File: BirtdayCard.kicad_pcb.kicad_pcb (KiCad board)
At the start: 2 copper layers, 26 parts, among them U2 0.763V~7V 4.2V~18V 3A, U3 ESP32-WROOM-32D-N4

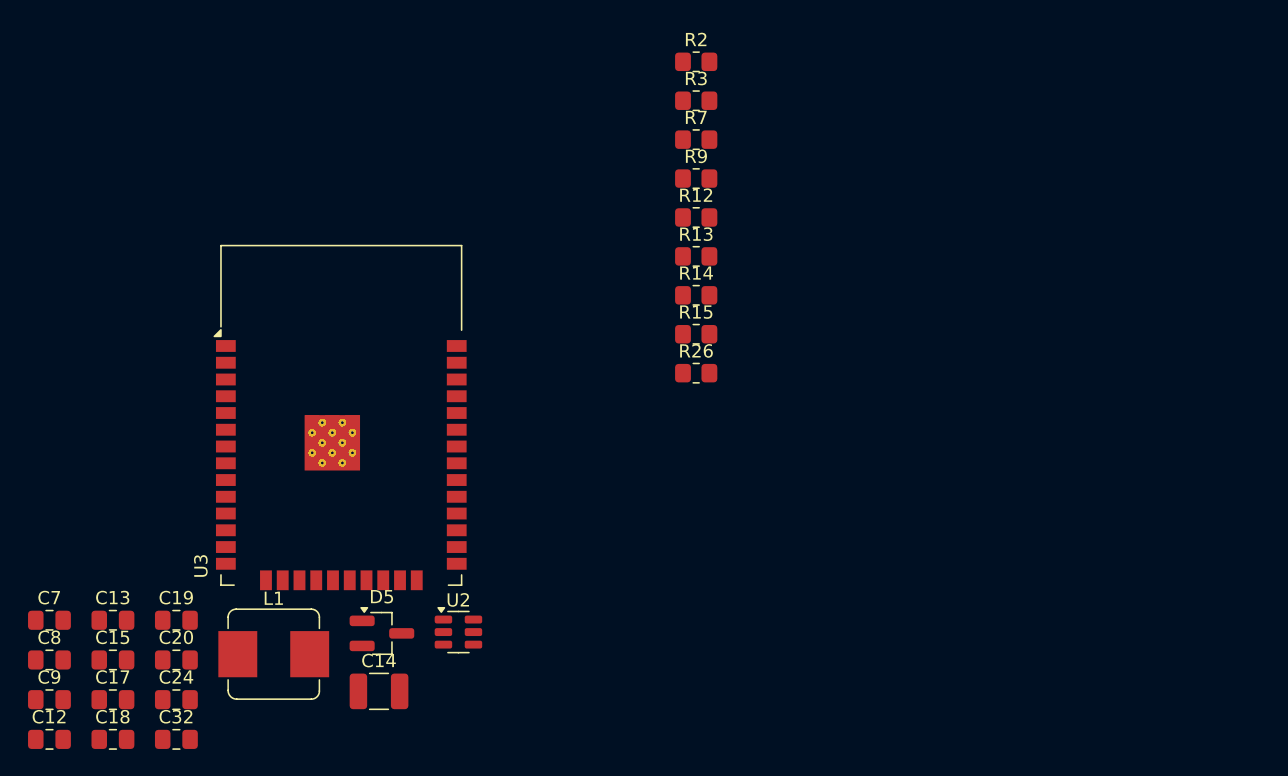
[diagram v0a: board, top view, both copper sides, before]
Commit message: adding components and consolidating with current parts
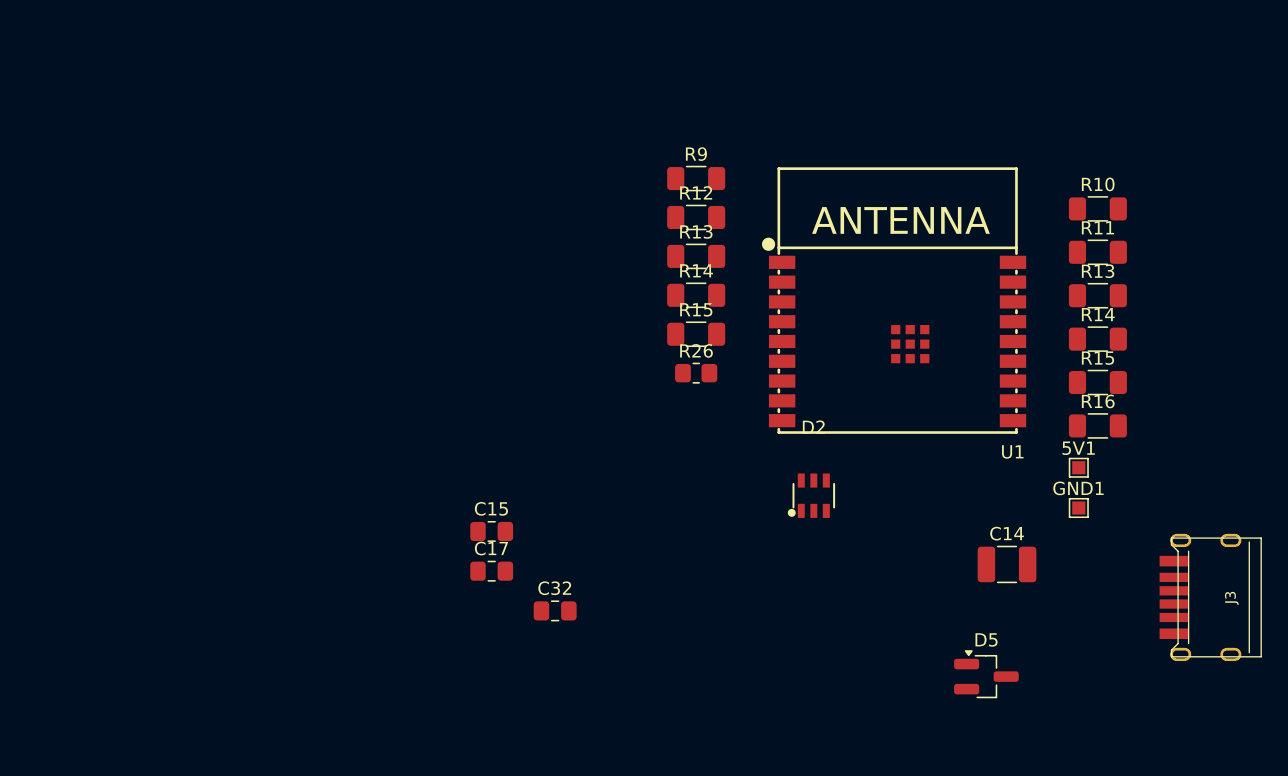
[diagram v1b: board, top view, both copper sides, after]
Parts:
- removed C12, C18, C19, C20, C7, C8: 10uF 25V, Capacitor_SMD:C_0805_2012Metric_Pad1.18x1.45mm_HandSolder
- removed C13: 470nF 50V, Capacitor_SMD:C_0805_2012Metric_Pad1.18x1.45mm_HandSolder
- removed C24, C9: 100nF 50V, Capacitor_SMD:C_0805_2012Metric_Pad1.18x1.45mm_HandSolder
- removed L1: 3.3uH 6A, Inductor_SMD:L_Bourns_SRP7028A_7.3x6.6mm
- removed R2: 33.2k, Resistor_SMD:R_0805_2012Metric_Pad1.20x1.40mm_HandSolder
- removed R3, R7: 10k, Resistor_SMD:R_0805_2012Metric_Pad1.20x1.40mm_HandSolder
- removed U2: 0.763V~7V 4.2V~18V 3A, Package_TO_SOT_SMD:TSOT-23-6
- removed U3: ESP32-WROOM-32D-N4, RF_Module:ESP32-WROOM-32
- added 5V1: 5V, TestPoint:TestPoint_Pad_1.0x1.0mm, F.Cu at (139.0, 79.7)
- added D2: USBLC6-2SC6, easyeda2kicad:SOT-23-6_L2.9-W1.6-P0.95-LS2.8-BL, F.Cu at (118.9, 81.8)
- added GND1: GND, TestPoint:TestPoint_Pad_1.0x1.0mm, F.Cu at (139.0, 82.7)
- added J3: USB_C_Receptacle_USB2.0, USB-C-Power-tester:TYPE-C-31-M-17_handsolder, F.Cu at (150.5, 89.5)
- added R10: 10k, Resistor_SMD:R_1206_3216Metric_Pad1.30x1.75mm_HandSolder, F.Cu at (140.4, 60.0)
- added R11: 10k, Resistor_SMD:R_1206_3216Metric_Pad1.30x1.75mm_HandSolder, F.Cu at (140.4, 63.3)
- added R13: 5k1, Resistor_SMD:R_1206_3216Metric_Pad1.30x1.75mm_HandSolder, F.Cu at (140.4, 66.6)
- added R14: 10k, Resistor_SMD:R_1206_3216Metric_Pad1.30x1.75mm_HandSolder, F.Cu at (140.4, 69.9)
- added R15: 10k, Resistor_SMD:R_1206_3216Metric_Pad1.30x1.75mm_HandSolder, F.Cu at (140.4, 73.2)
- added R16: 5k1, Resistor_SMD:R_1206_3216Metric_Pad1.30x1.75mm_HandSolder, F.Cu at (140.4, 76.5)
- added U1: ESP32-C3-WROOM-02-N4(4MB), easyeda2kicad:BULETM-SMD_ESPRESSIF_ESP32-C3-WROOM-02-N4-4MB, F.Cu at (125.3, 70.1)
- R12, R9: footprint Resistor_SMD:R_0805_2012Metric_Pad1.20x1.40mm_HandSolder -> Resistor_SMD:R_1206_3216Metric_Pad1.30x1.75mm_HandSolder
- R13: value 10k -> 5k1; footprint Resistor_SMD:R_0805_2012Metric_Pad1.20x1.40mm_HandSolder -> Resistor_SMD:R_1206_3216Metric_Pad1.30x1.75mm_HandSolder
- R14, R15: value 4.7k -> 10k; footprint Resistor_SMD:R_0805_2012Metric_Pad1.20x1.40mm_HandSolder -> Resistor_SMD:R_1206_3216Metric_Pad1.30x1.75mm_HandSolder
- moved C14 48.6 mm to (133.6, 87.0)
- moved D5 45.9 mm to (132.0, 95.5)
- moved C32 30.3 mm to (99.3, 90.5)
- moved C15 30.3 mm to (94.5, 84.5)
- moved C17 30.3 mm to (94.5, 87.5)
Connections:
- D5 pad 1: GPIO22 -> GPIO7
- D5 pad 2: GPIO21 -> GPIO6
- R12 pad 2: GPIO13 -> GPIO3
- R13 pad 1: GPIO0 -> GND
- R13 pad 2: +3V3 -> Net-(J3-CC1)
- R14 pad 1: GPIO22 -> +3V3
- R14 pad 2: +3V3 -> GPIO8
- R15 pad 1: GPIO21 -> +3V3
- R15 pad 2: +3V3 -> ESP_EN

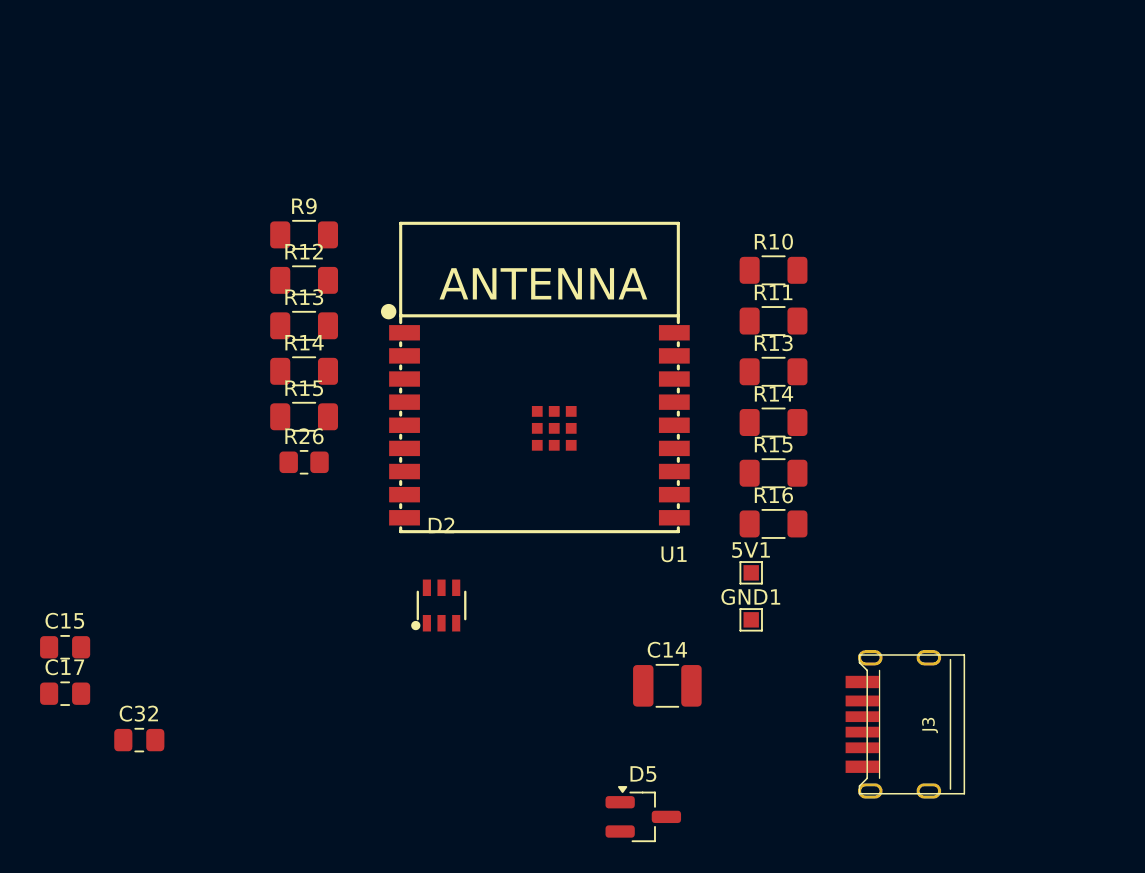
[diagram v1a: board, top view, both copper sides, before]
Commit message: USB configured and added LDO
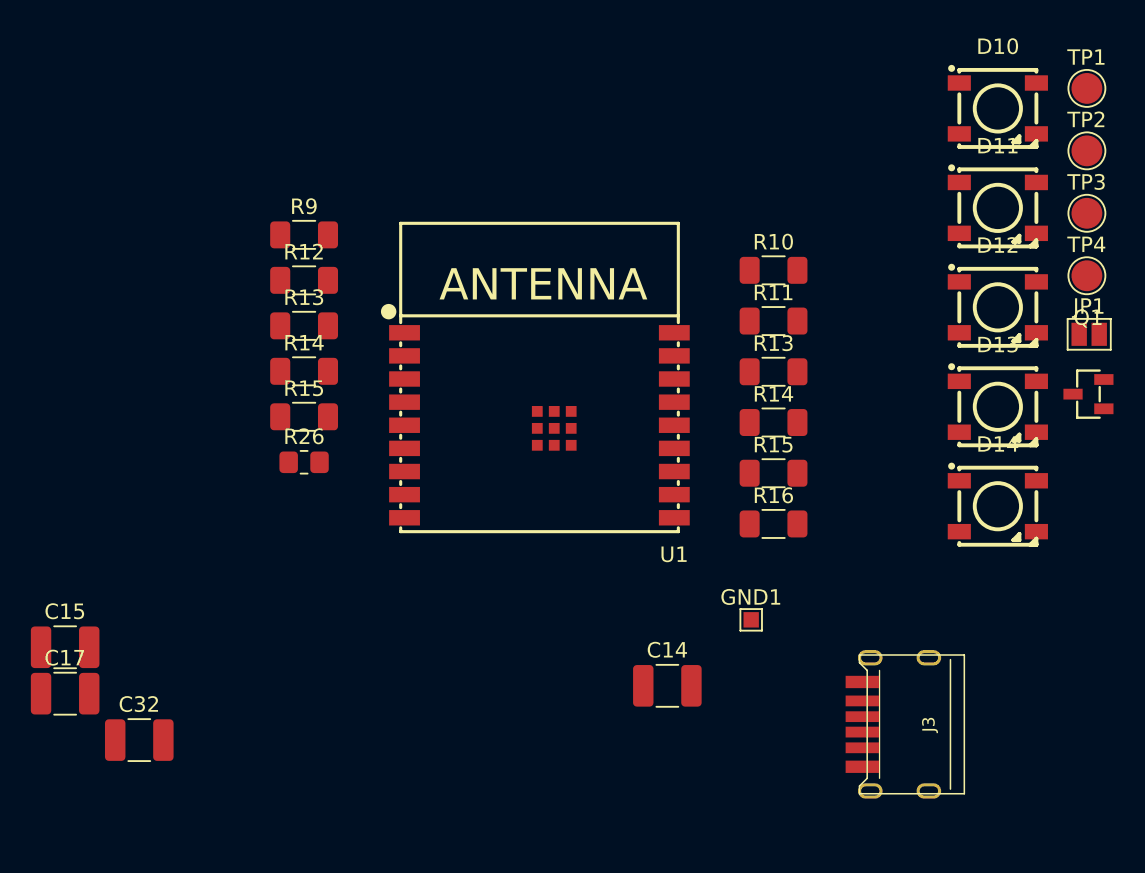
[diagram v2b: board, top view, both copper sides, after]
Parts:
- removed 5V1: 5V, TestPoint:TestPoint_Pad_1.0x1.0mm
- removed D2: USBLC6-2SC6, easyeda2kicad:SOT-23-6_L2.9-W1.6-P0.95-LS2.8-BL
- removed D5: 7A 150W, Package_TO_SOT_SMD:SOT-23_Handsoldering
- added D10: WS2812B, easyeda2kicad:LED-SMD_4P-L5.0-W5.0-BL_TC5050RGB, F.Cu at (155.0, 49.5)
- added D11: WS2812B, easyeda2kicad:LED-SMD_4P-L5.0-W5.0-BL_TC5050RGB, F.Cu at (155.0, 56.0)
- added D12: WS2812B, easyeda2kicad:LED-SMD_4P-L5.0-W5.0-BL_TC5050RGB, F.Cu at (155.0, 62.5)
- added D13: WS2812B, easyeda2kicad:LED-SMD_4P-L5.0-W5.0-BL_TC5050RGB, F.Cu at (155.0, 68.9)
- added D14: WS2812B, easyeda2kicad:LED-SMD_4P-L5.0-W5.0-BL_TC5050RGB, F.Cu at (155.0, 75.3)
- added JP1: SolderJumper_2_Open, Jumper:SolderJumper-2_P1.3mm_Open_Pad1.0x1.5mm, F.Cu at (160.9, 64.2)
- added Q1: 2N7002_C306856, easyeda2kicad:SOT-23-3_L2.9-W1.3-P1.90-LS2.4-BR, F.Cu at (160.9, 68.1)
- added TP1: TestPoint_Probe, TestPoint:TestPoint_Pad_D2.0mm, F.Cu at (160.8, 48.2)
- added TP2: TestPoint_Probe, TestPoint:TestPoint_Pad_D2.0mm, F.Cu at (160.8, 52.3)
- added TP3: TestPoint_Probe, TestPoint:TestPoint_Pad_D2.0mm, F.Cu at (160.8, 56.4)
- added TP4: TestPoint_Probe, TestPoint:TestPoint_Pad_D2.0mm, F.Cu at (160.8, 60.4)
- C15, C17, C32: footprint Capacitor_SMD:C_0805_2012Metric_Pad1.18x1.45mm_HandSolder -> Capacitor_SMD:C_1210_3225Metric_Pad1.33x2.70mm_HandSolder
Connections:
- J3 pad A12: (no net) -> GND
- J3 pad A5: (no net) -> Net-(J3-CC1)
- J3 pad A9: (no net) -> +5V
- J3 pad B12: (no net) -> GND
- J3 pad B5: (no net) -> Net-(J3-CC2)
- J3 pad B9: (no net) -> +5V

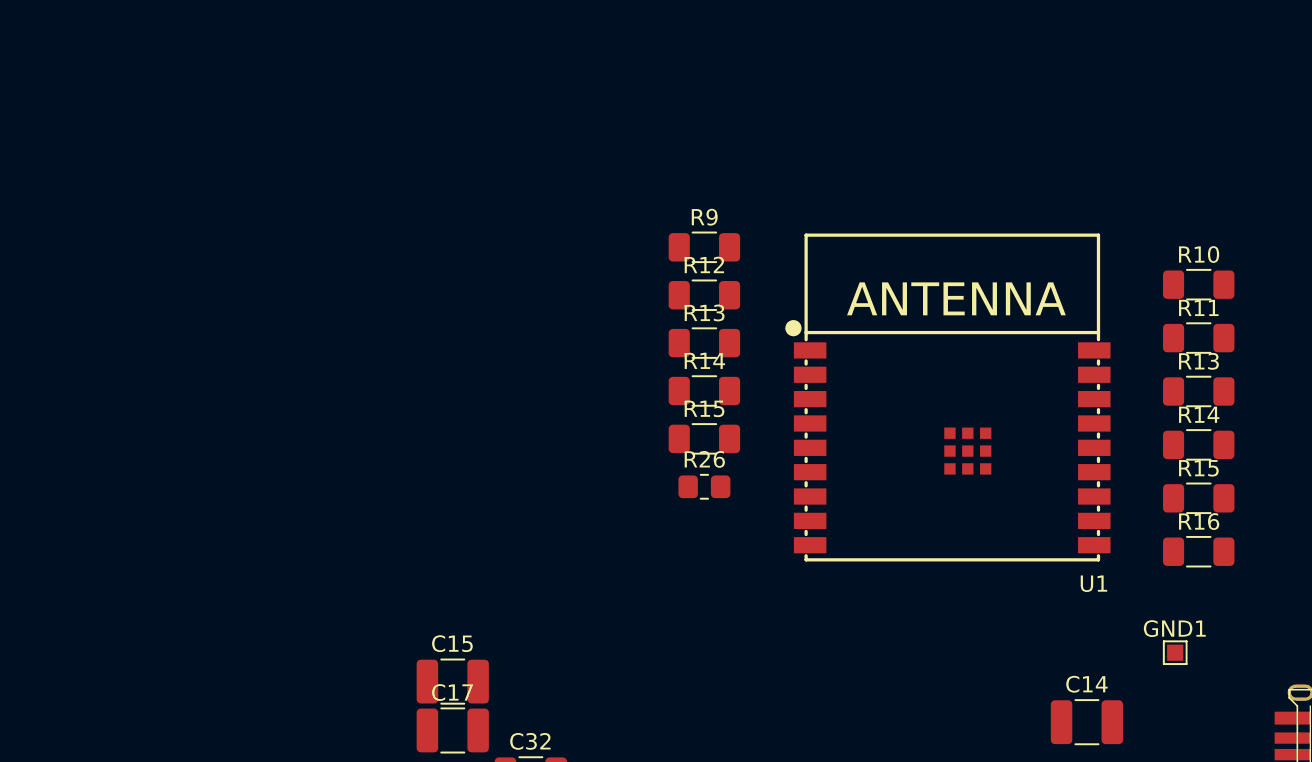
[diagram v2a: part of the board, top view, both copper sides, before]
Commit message: General layout improvements, added ESD protection and more LEDS
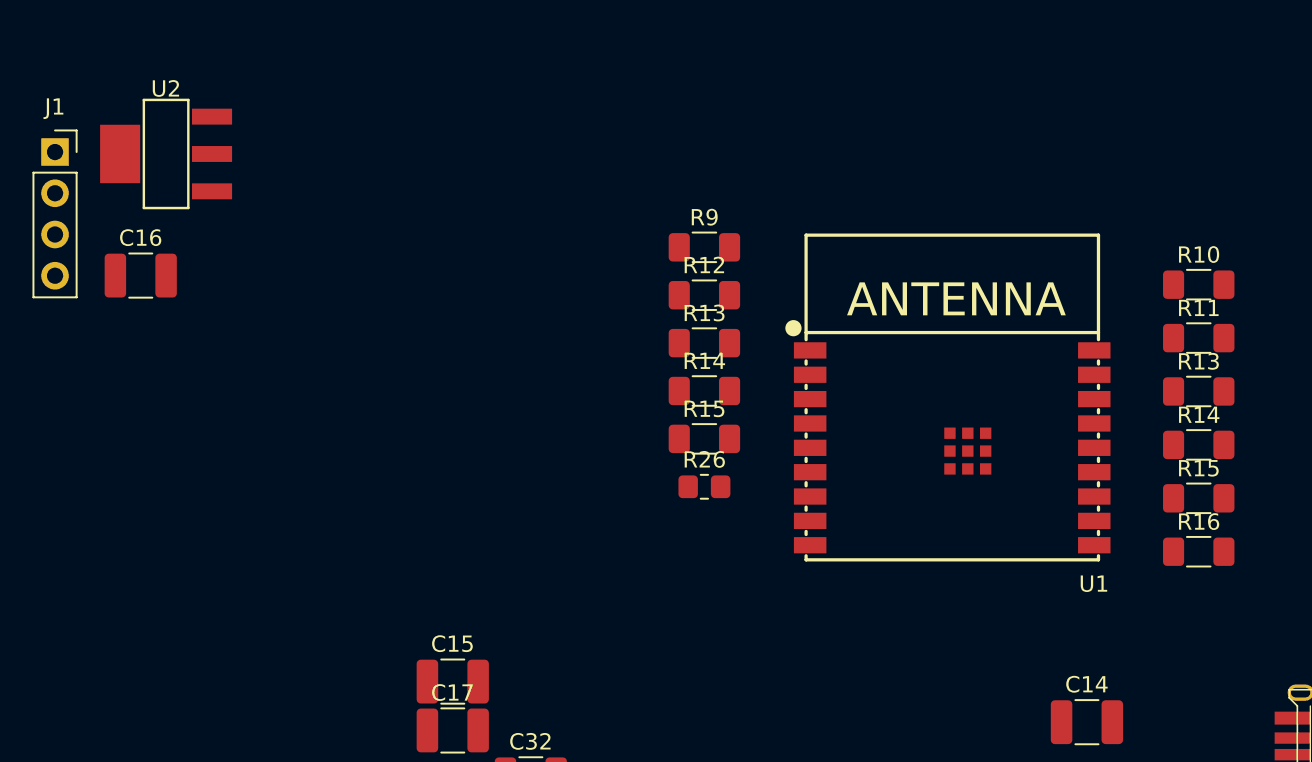
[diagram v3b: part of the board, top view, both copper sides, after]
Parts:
- removed GND1: GND, TestPoint:TestPoint_Pad_1.0x1.0mm
- added C16: 47uF 10V, Capacitor_SMD:C_1210_3225Metric_Pad1.33x2.70mm_HandSolder, F.Cu at (75.3, 59.5)
- added J1: Conn_01x04_Socket, Connector_PinSocket_2.54mm:PinSocket_1x04_P2.54mm_Vertical, F.Cu at (70.0, 51.9)
- added U2: AMS1117-3.3_C347222, easyeda2kicad:SOT-223-4_L6.5-W3.5-P2.30-LS7.0-BR, F.Cu at (76.8, 52.0)

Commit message: archived 3D models
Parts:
- added C33: 100nF 50V, Capacitor_SMD:C_1210_3225Metric_Pad1.33x2.70mm_HandSolder, F.Cu at (134.6, 105.8)
- added D15: WS2812B, easyeda2kicad:LED-SMD_4P-L5.0-W5.0-BL_TC5050RGB, F.Cu at (111.5, 97.7)
- added D16: WS2812B, easyeda2kicad:LED-SMD_4P-L5.0-W5.0-BL_TC5050RGB, F.Cu at (111.5, 104.7)
- added D17: WS2812B, easyeda2kicad:LED-SMD_4P-L5.0-W5.0-BL_TC5050RGB, F.Cu at (111.5, 111.8)
- added D18: WS2812B, easyeda2kicad:LED-SMD_4P-L5.0-W5.0-BL_TC5050RGB, F.Cu at (111.5, 118.8)
- added D19: WS2812B, easyeda2kicad:LED-SMD_4P-L5.0-W5.0-BL_TC5050RGB, F.Cu at (111.5, 125.8)
- added D20: WS2812B, easyeda2kicad:LED-SMD_4P-L5.0-W5.0-BL_TC5050RGB, F.Cu at (119.5, 97.7)
- added D21: WS2812B, easyeda2kicad:LED-SMD_4P-L5.0-W5.0-BL_TC5050RGB, F.Cu at (119.5, 104.7)
- added D22: WS2812B, easyeda2kicad:LED-SMD_4P-L5.0-W5.0-BL_TC5050RGB, F.Cu at (119.5, 111.8)
- added D23: WS2812B, easyeda2kicad:LED-SMD_4P-L5.0-W5.0-BL_TC5050RGB, F.Cu at (119.5, 118.8)
- added D24: WS2812B, easyeda2kicad:LED-SMD_4P-L5.0-W5.0-BL_TC5050RGB, F.Cu at (119.5, 125.8)
- added D25: WS2812B, easyeda2kicad:LED-SMD_4P-L5.0-W5.0-BL_TC5050RGB, F.Cu at (127.5, 97.7)
- added D26: WS2812B, easyeda2kicad:LED-SMD_4P-L5.0-W5.0-BL_TC5050RGB, F.Cu at (127.5, 104.7)
- added D27: WS2812B, easyeda2kicad:LED-SMD_4P-L5.0-W5.0-BL_TC5050RGB, F.Cu at (127.5, 111.8)
- added D5: 7A 150W, Package_TO_SOT_SMD:SOT-23_Handsoldering, F.Cu at (134.8, 96.6)
- added D6: 7A 150W, Package_TO_SOT_SMD:SOT-23_Handsoldering, F.Cu at (134.8, 101.4)
- added JP2: SolderJumper_3_Open, Jumper:SolderJumper-3_P1.3mm_Open_RoundedPad1.0x1.5mm, F.Cu at (134.4, 109.7)
- J3: footprint USB-C-Power-tester:TYPE-C-31-M-17_handsolder -> easyeda2kicad:TYPE-C-SMD_TYPE-C-6P_5
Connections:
- D14 pad 2: unconnected-(D14-DOUT-Pad2) -> Net-(D14-DOUT)
- R14 pad 1: +3V3 -> GPIO8 (x2)
- R14 pad 2: GPIO8 -> Net-(JP2-C) (x2)
- U1 pad 10: GPIO10 -> BUZZ
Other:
- board outline added: 99 x 99 mm

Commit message: added buzzer components and pwr LED
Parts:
- added LED2: FC-3215HRK-620D, easyeda2kicad:LED1206-R-RD_RED, F.Cu at (108.0, 48.4)
- added LS1: KSSGK4B16-20, Library:Buzzer KSSGK4B16-20, F.Cu at (110.0, 42.0)
- added R17: 1k, Resistor_SMD:R_1206_3216Metric_Pad1.30x1.75mm_HandSolder, F.Cu at (118.0, 38.4)
- added R18: 1k, Resistor_SMD:R_1206_3216Metric_Pad1.30x1.75mm_HandSolder, F.Cu at (118.0, 41.7)
- added R19: 1k, Resistor_SMD:R_1206_3216Metric_Pad1.30x1.75mm_HandSolder, F.Cu at (118.0, 45.0)

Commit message: Starting PCB design
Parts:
- added KEY1: DTSM-61R-V-T/R, easyeda2kicad:KEY-SMD_4P-L6.2-W6.2-P4.50-LS9.0, F.Cu at (198.7, 43.0)
- added KEY2: DTSM-61R-V-T/R, easyeda2kicad:KEY-SMD_4P-L6.2-W6.2-P4.50-LS9.0, F.Cu at (197.7, 54.5)
- added TP5: TestPoint_Probe, TestPoint:TestPoint_Pad_D2.0mm, F.Cu at (206.0, 41.3)
- added TP6: TestPoint_Probe, TestPoint:TestPoint_Pad_D2.0mm, F.Cu at (206.0, 45.4)
- moved D10 106.3 mm to (261.2, 44.5)
- moved D11 106.3 mm to (261.2, 51.0)
- moved D12 106.3 mm to (261.2, 57.5)
- moved D13 106.3 mm to (261.2, 63.9)
- moved D14 106.3 mm to (261.2, 70.3)
- moved Q1 106.3 mm to (267.0, 63.1)
- moved R10 106.3 mm to (246.6, 55.0)
- moved R11 106.3 mm to (246.6, 58.3)
- moved R13 106.3 mm to (246.6, 61.6)
- moved R14 106.3 mm to (246.6, 64.9)
- moved R15 106.3 mm to (246.6, 68.2)
- moved R16 106.3 mm to (246.6, 71.5)
- moved D15 106.3 mm to (217.6, 92.7)
- moved D16 106.3 mm to (217.6, 99.7)
- moved D17 106.3 mm to (217.6, 106.8)
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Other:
- board text added: "18"
- board text added: "Lieve Sander,"

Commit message: Enlarged PCB and working on text
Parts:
- removed R26: 220, Resistor_SMD:R_0805_2012Metric_Pad1.20x1.40mm_HandSolder
- removed TP5, TP6: TestPoint_Probe, TestPoint:TestPoint_Pad_D2.0mm
- added F1: Fuse_Small 2A, Fuse:Fuse_1206_3216Metric_Pad1.42x1.75mm_HandSolder, F.Cu at (142.5, 110.3)
- added J2: Conn_01x05_Pin, Connector_PinSocket_2.54mm:PinSocket_1x05_P2.54mm_Horizontal, F.Cu at (134.5, 89.1)
- added REF**: OSHW-Logo_11.4x12mm_SilkScreen, Symbol:OSHW-Logo_11.4x12mm_SilkScreen, B.Cu at (133.0, 171.0)
- added REF**: KiCad-Logo2_12mm_SilkScreen, Symbol:KiCad-Logo2_12mm_SilkScreen, B.Cu at (158.5, 168.5)
- moved D10 107.9 mm to (157.1, 73.3)
- moved D11 107.9 mm to (157.1, 79.8)
- moved D12 107.9 mm to (157.1, 86.2)
- moved D13 107.9 mm to (157.1, 92.7)
- moved D14 107.9 mm to (157.1, 99.1)
- moved Q1 107.9 mm to (163.0, 91.8)
- moved D15 107.9 mm to (113.6, 121.4)
- moved D16 107.9 mm to (113.6, 128.5)
- moved D17 107.9 mm to (113.6, 135.5)
- moved D18 107.9 mm to (113.6, 142.6)
- moved D19 107.9 mm to (113.6, 149.6)
- moved LS1 107.9 mm to (112.1, 65.8)
- moved R17 107.9 mm to (120.1, 62.1)
- moved R18 107.9 mm to (120.1, 65.5)
- moved R19 107.9 mm to (120.1, 68.8)
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- renumbered J1 to H1
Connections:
- J3 pad A9: +5V -> Net-(F1-Pad1)
- J3 pad B9: +5V -> Net-(F1-Pad1)
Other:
- board size 99 x 99 mm -> 150 x 150 mm
- board text added: "Lieve Sander, Wauw, 18 jaar oud! Nu ben je officieel volwassen, wat betekent dat je allemaal nieuwe features hebt unlocked in de gezamenlijke server. Even op een rijtje: 1. Full access to the worldmap 2. Een eigen stem (waar misschien naar wordt geluisterd!) 3. Je eigen zorgverZEKERING én andere vaste lasten! 4. Toegang tot de vierwielige fatbike crusher (wanneer je een plastic kaartje hebt gesco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"
- board text removed: "Lieve Sander,"
